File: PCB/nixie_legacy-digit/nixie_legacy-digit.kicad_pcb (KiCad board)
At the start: 2 copper layers, 50.8 x 78.7 mm, 12 parts, among them J1 HEADER_16

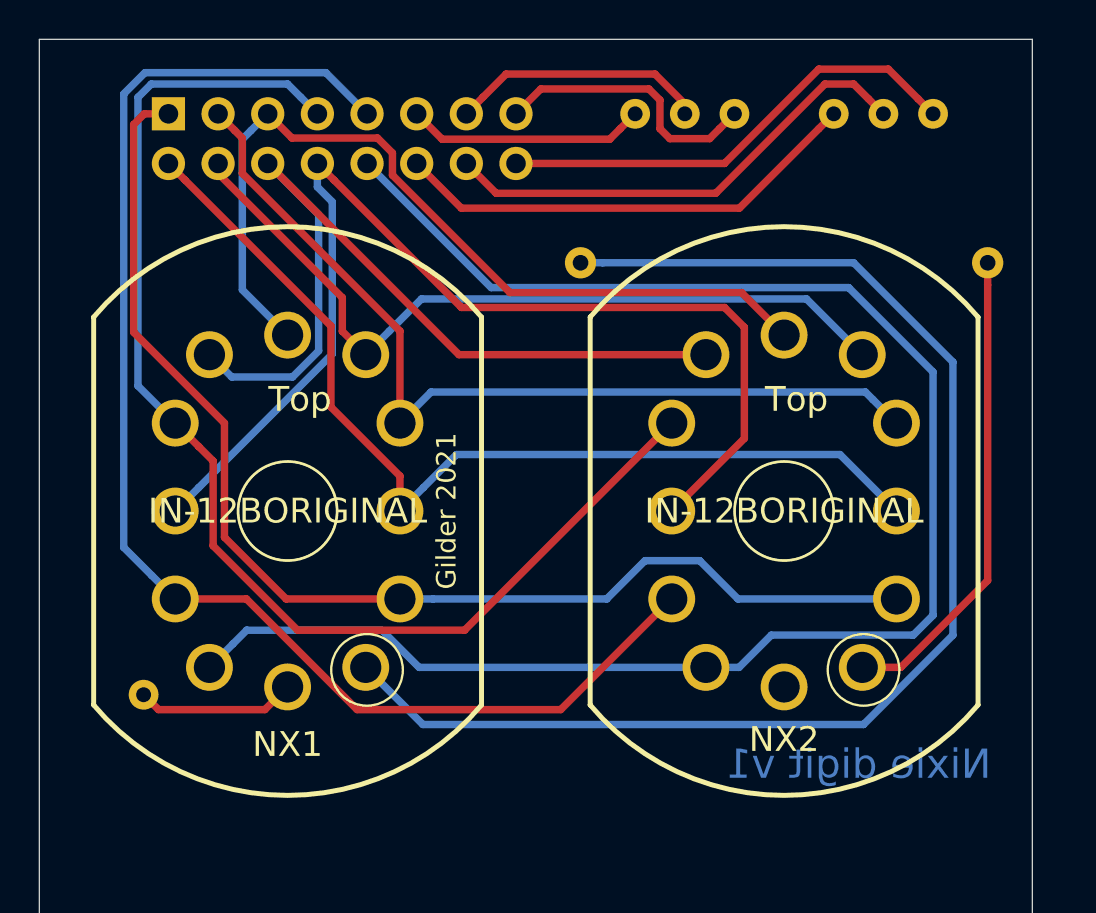
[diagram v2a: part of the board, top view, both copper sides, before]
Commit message: -power board: updated 7805 footprint to better fit piece, "A55" instead of "A56", 9v input pad shape swap so that ground makes sense -digit board: added resistor value, vertical connector, correct pinout for rear mounting to match header population on demux board -new_rtc_pcbHack: deprecated. works with v1 of digit boards (with bad header pinout) but no longer needed. did not update with time demux, only displayed idle animation and set menu
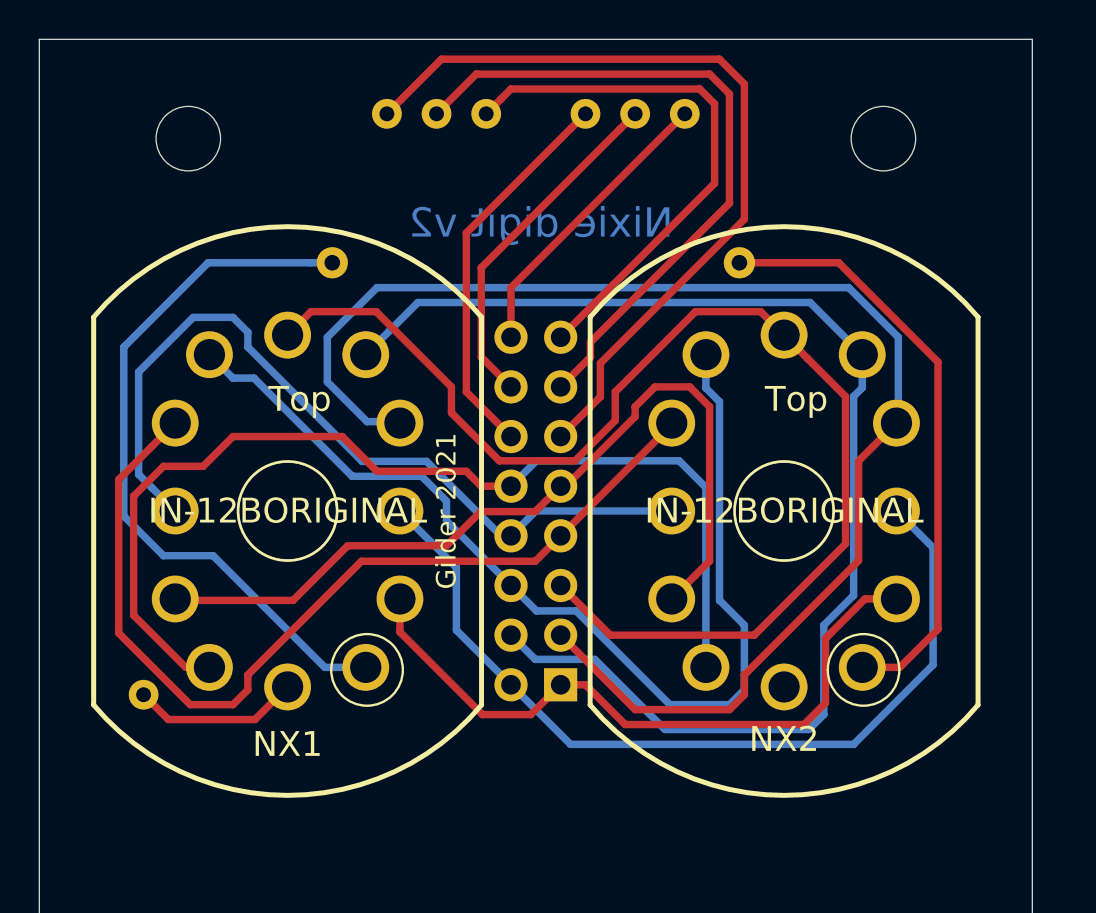
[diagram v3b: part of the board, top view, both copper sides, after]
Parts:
- removed J1: HEADER_16, Connector_PinHeader_2.54mm:PinHeader_2x08_P2.54mm_Vertical
- removed R1, R2: 20k, Resistor_THT:R_Axial_DIN0207_L6.3mm_D2.5mm_P7.62mm_Horizontal
- added "0": HEADER_16, Connector_PinHeader_2.54mm:PinHeader_2x08_P2.54mm_Vertical, B.Cu at (100.3, 118.1)
- added R 20k: 20k, Resistor_THT:R_Axial_DIN0207_L6.3mm_D2.5mm_P7.62mm_Horizontal, B.Cu at (112.0, 88.9)
- added R 20k: 20k, Resistor_THT:R_Axial_DIN0207_L6.3mm_D2.5mm_P7.62mm_Horizontal, B.Cu at (91.2, 88.9)
- moved hr0 12.7 mm to (104.1, 88.9)
- moved hr10 12.7 mm to (94.0, 88.9)
- moved min10 12.7 mm to (96.5, 88.9)
- moved sec0 12.7 mm to (109.2, 88.9)
- moved sec10 12.7 mm to (99.1, 88.9)
- moved min0 12.7 mm to (106.7, 88.9)
- renumbered dp to DP
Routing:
- net 1: track 85.5 -> 53.3 mm
- net Net-(NX1-PadA): track 68.3 -> 36.7 mm
- net digit1msb: track 12.3 -> 41.9 mm
- net 2: track 70.8 -> 43.3 mm
- net 0: track 62.4 -> 34.9 mm
- net 8: track 46.4 -> 71.0 mm
- net 7: track 40.7 -> 65.2 mm
- net digit3: track 13.2 -> 35.3 mm
- net 6: track 44.6 -> 63.9 mm
- net 4: track 64.3 -> 48.2 mm
- net 3: track 57.7 -> 41.9 mm
- net digit5: track 14.1 -> 27.7 mm
- net 5: track 43.7 -> 53.6 mm
- net digit6lsb: track 24.3 -> 15.1 mm
- net digit4: track 24.9 -> 17.9 mm
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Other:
- outline, holes or cut-outs redrawn
- board text added: "Nixie digit v2"
- board text removed: "Nixie digit v1"
